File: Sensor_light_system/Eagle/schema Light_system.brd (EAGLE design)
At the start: 80.1 x 49.8 mm, 4 parts

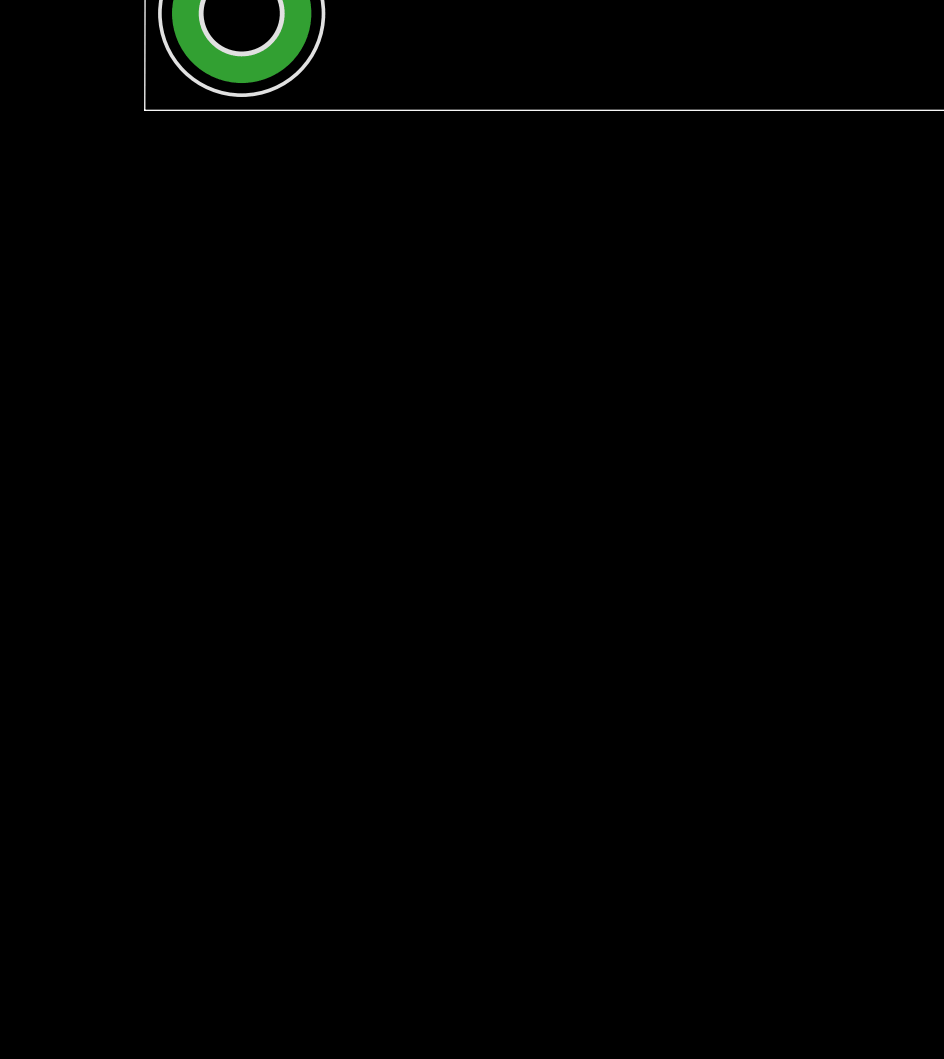
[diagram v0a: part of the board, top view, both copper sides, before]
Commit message: schema sensor aangepast
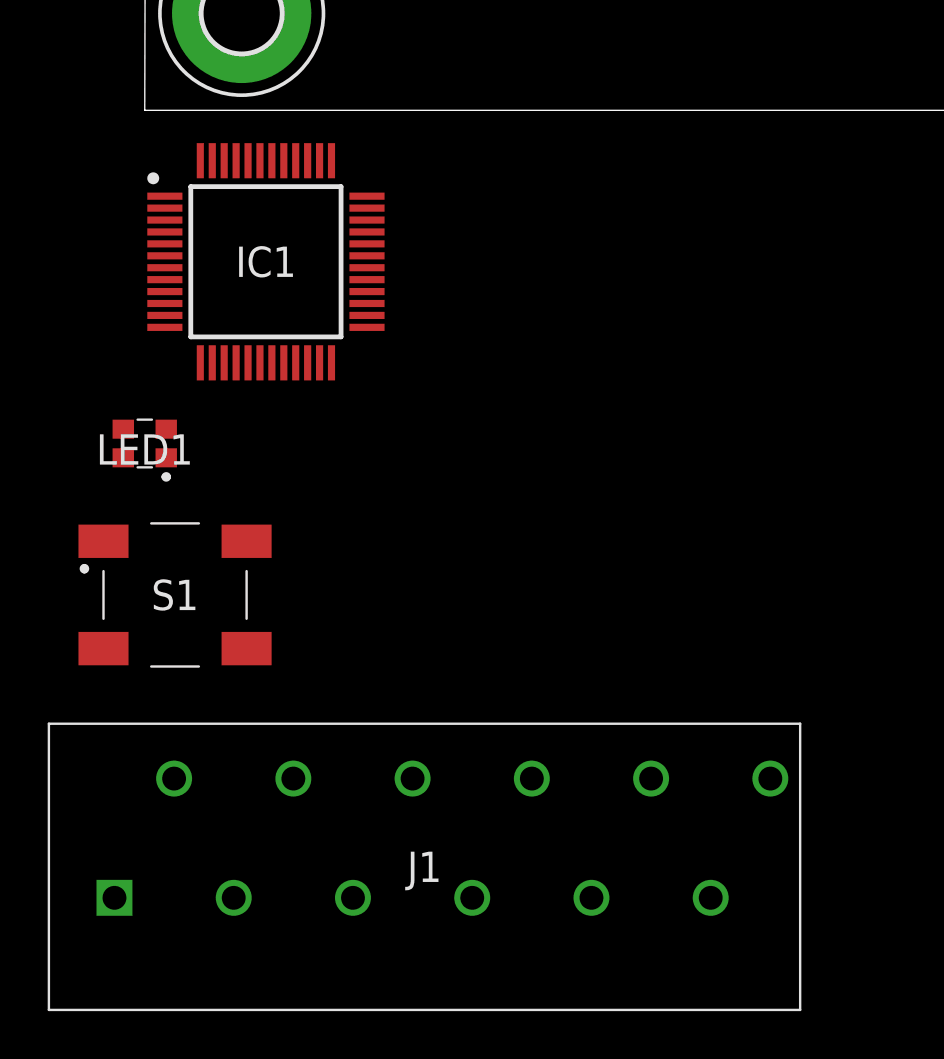
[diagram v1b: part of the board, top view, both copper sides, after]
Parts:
- added IC1: STM32F030C8T6TR, Library light system:QFP50P900X900X160-48N
- added J1: 12_WAY_CON, Library light system:1990106
- added LED1: RGB_LED, Library light system:ASMBKTF00A306
- added S1: PUSH_BUTTON, Library light system:LL3301FF065QJ
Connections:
- new net +3V3: IC1.1, IC1.48
- new net GND: IC1.23
- new net VDDA: IC1.9
- new net VDD_2: IC1.24
- new net VSSA: IC1.8
- new net VSS_2: IC1.47
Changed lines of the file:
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@@
 <element name="H3" library="holes" library_urn="urn:adsk.eagle:library:237" package="3,3-PAD" package3d_urn="urn:adsk.eagle:package:14283/1" value="MOUNT-PAD-ROUND3.3" x="4.064" y="4.064"/>
 <element name="H4" library="holes" library_urn="urn:adsk.eagle:library:237" package="3,3-PAD" package3d_urn="urn:adsk.eagle:package:14283/1" value="MOUNT-PAD-ROUND3.3" x="75.946" y="3.937"/>
+<element name="IC1" library="Library light system" package="QFP50P900X900X160-48N" value="STM32F030C8T6TR" x="5.08" y="-6.35">
+<attribute name="DESCRIPTION" value="32-Bit MCU Cortex-M0 64K Flash LQFP48 32-Bit MCU Cortex-M0 64K Flash LQFP48" x="5.08" y="-6.35" size="1.778" layer="27" display="off"/>
+<attribute name="HEIGHT" value="1.6mm" x="5.08" y="-6.35" size="1.778" layer="27" display="off"/>
+<attribute name="MANUFACTURER_NAME" value="STMicroelectronics" x="5.08" y="-6.35" size="1.778" layer="27" display="off"/>
+<attribute name="MANUFACTURER_PART_NUMBER" value="STM32F030C8T6TR" x="5.08" y="-6.35" size="1.778" layer="27" display="off"/>
+<attribute name="MOUSER_PART_NUMBER" value="511-STM32F030C8T6TR" x="5.08" y="-6.35" size="1.778" layer="27" display="off"/>
+<attribute name="MOUSER_PRICE-STOCK" value="https://www.mouser.com/Search/Refine.aspx?Keyword=511-STM32F030C8T6TR" x="5.08" y="-6.35" size="1.778" layer="27" display="off"/>
+<attribute name="NAME" x="5.08" y="-6.35" size="1.27" layer="25" align="center"/>
+<attribute name="VALUE" x="5.08" y="-6.35" size="1.27" layer="27" align="center"/>
+</element>
+<element name="LED1" library="Library light system" package="ASMBKTF00A306" value="RGB_LED" x="0" y="-13.97">
+<attribute name="DESCRIPTION" value="Standard LEDs - SMD 2220 PLCC4 Tricolor" x="0" y="-13.97" size="1.778" layer="27" display="off"/>
+<attribute name="HEIGHT" value="2.1mm" x="0" y="-13.97" size="1.778" layer="27" display="off"/>
+<attribute name="MANUFACTURER_NAME" value="Avago Technologies" x="0" y="-13.97" size="1.778" layer="27" display="off"/>
+<attribute name="MANUFACTURER_PART_NUMBER" value="ASMB-KTF0-0A306" x="0" y="-13.97" size="1.778" layer="27" display="off"/>
+<attribute name="MOUSER_PART_NUMBER" value="630-ASMB-KTF0-0A306" x="0" y="-13.97" size="1.778" layer="27" display="off"/>
+<attribute name="MOUSER_PRICE-STOCK" value="https://www.mouser.com/Search/Refine.aspx?Keyword=630-ASMB-KTF0-0A306" x="0" y="-13.97" size="1.778" layer="27" display="off"/>
+<attribute name="NAME" x="0" y="-14.22" size="1.27" layer="25" align="center"/>
+<attribute name="VALUE" x="0" y="-14.22" size="1.27" layer="27" align="center"/>
+</element>
+<element name="S1" library="Library light system" package="LL3301FF065QJ" value="PUSH_BUTTON" x="1.27" y="-20.32">
+<attribute name="DESCRIPTION" value="Pushbutton Switches 50mA 12VDC F065 7.0mm J-Lead" x="1.27" y="-20.32" size="1.778" layer="27" display="off"/>
+<attribute name="HEIGHT" value="7.3mm" x="1.27" y="-20.32" size="1.778" layer="27" display="off"/>
+<attribute name="MANUFACTURER_NAME" value="E-Switch" x="1.27" y="-20.32" size="1.778" layer="27" display="off"/>
+<attribute name="MANUFACTURER_PART_NUMBER" value="LL3301FF065QJ" x="1.27" y="-20.32" size="1.778" layer="27" display="off"/>
+<attribute name="MOUSER_PART_NUMBER" value="612-LL3301FF065QJ" x="1.27" y="-20.32" size="1.778" layer="27" display="off"/>
+<attribute name="MOUSER_PRICE-STOCK" value="https://www.mouser.com/Search/Refine.aspx?Keyword=612-LL3301FF065QJ" x="1.27" y="-20.32" size="1.778" layer="27" display="off"/>
+<attribute name="NAME" x="1.27" y="-20.32" size="1.27" layer="25" align="center"/>
+<attribute name="VALUE" x="1.27" y="-20.32" size="1.27" layer="27" align="center"/>
+</element>
+<element name="J1" library="Library light system" package="1990106" value="12_WAY_CON" x="-1.27" y="-33.02">
+<attribute name="DESCRIPTION" value="PTSA 0,5/12-2,5-Z" x="-1.27" y="-33.02" size="1.778" layer="27" display="off"/>
+<attribute name="HEIGHT" value="13.1mm" x="-1.27" y="-33.02" size="1.778" layer="27" display="off"/>
+<attribute name="MANUFACTURER_NAME" value="Phoenix Contact" x="-1.27" y="-33.02" size="1.778" layer="27" display="off"/>
+<attribute name="MANUFACTURER_PART_NUMBER" value="1990106" x="-1.27" y="-33.02" size="1.778" layer="27" display="off"/>
+<attribute name="MOUSER_PART_NUMBER" value="651-1990106" x="-1.27" y="-33.02" size="1.778" layer="27" display="off"/>
+<attribute name="MOUSER_PRICE-STOCK" value="https://www.mouser.com/Search/Refine.aspx?Keyword=651-1990106" x="-1.27" y="-33.02" size="1.778" layer="27" display="off"/>
+<attribute name="NAME" x="11.73" y="-31.72" size="1.27" layer="25" align="center"/>
+<attribute name="VALUE" x="11.73" y="-31.72" size="1.27" layer="27" align="center"/>
+</element>
 </elements>
 <signals>
+<signal name="VSSA">
+<contactref element="IC1" pad="8"/>
+</signal>
+<signal name="VDDA">
+<contactref element="IC1" pad="9"/>
+</signal>
+<signal name="VDD_2">
+<contactref element="IC1" pad="24"/>
+</signal>
+<signal name="VSS_2">
+<contactref element="IC1" pad="47"/>
+</signal>
+<signal name="+3V3">
+<contactref element="IC1" pad="1"/>
+<contactref element="IC1" pad="48"/>
+<wire x1="2.33" y1="-2.112" x2="0.842" y2="-3.6" width="0" layer="19" extent="1-1"/>
+</signal>
+<signal name="GND">
+<contactref element="IC1" pad="23"/>
+</signal>
 </signals>
 <mfgpreviewcolors>

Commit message: schema sensoren
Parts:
- added JP1, JP2, JP3: (no value), jumper:JP4Q
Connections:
- removed net VDDA: IC1.9
- removed net VDD_2: IC1.24
- removed net VSSA: IC1.8
- removed net VSS_2: IC1.47
- new net N$3: IC1.7, S1.3, S1.4
- net +3V3: now also IC1.24, IC1.9
- net GND: now also IC1.47, IC1.8, S1.1, S1.2
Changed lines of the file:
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@@
 <?xml version="1.0" encoding="utf-8"?>
 <!DOCTYPE eagle SYSTEM "eagle.dtd">
-<eagle version="9.2.0">
+<eagle version="8.0.2">
 <drawing>
 <settings>
 <setting alwaysvectorfont="yes"/>
-<setting keepoldvectorfont="yes"/>
 <setting verticaltext="up"/>
 </settings>
@@
 <param name="dpMaxLengthDifference" value="10mm"/>
 <param name="dpGapFactor" value="2.5"/>
+<param name="checkGrid" value="0"/>
 <param name="checkAngle" value="0"/>
 <param name="checkFont" value="1"/>
 <param name="checkRestrict" value="1"/>
-<param name="checkStop" value="0"/>
-<param name="checkValues" value="0"/>
-<param name="checkNames" value="1"/>
-<param name="checkWireStubs" value="1"/>
-<param name="checkPolygonWidth" value="0"/>
 <param name="useDiameter" value="13"/>
 <param name="maxErrors" value="50"/>
@@
 </autorouter>
 <elements>
-<element name="H1" library="holes" library_urn="urn:adsk.eagle:library:237" package="3,3-PAD" package3d_urn="urn:adsk.eagle:package:14283/1" value="MOUNT-PAD-ROUND3.3" x="4.064" y="45.847"/>
-<element name="H2" library="holes" library_urn="urn:adsk.eagle:library:237" package="3,3-PAD" package3d_urn="urn:adsk.eagle:package:14283/1" value="MOUNT-PAD-ROUND3.3" x="76.073" y="45.72"/>
-<element name="H3" library="holes" library_urn="urn:adsk.eagle:library:237" package="3,3-PAD" package3d_urn="urn:adsk.eagle:package:14283/1" value="MOUNT-PAD-ROUND3.3" x="4.064" y="4.064"/>
-<element name="H4" library="holes" library_urn="urn:adsk.eagle:library:237" package="3,3-PAD" package3d_urn="urn:adsk.eagle:package:14283/1" value="MOUNT-PAD-ROUND3.3" x="75.946" y="3.937"/>
+<element name="H1" library="holes" package="3,3-PAD" value="MOUNT-PAD-ROUND3.3" x="4.064" y="45.847"/>
+<element name="H2" library="holes" package="3,3-PAD" value="MOUNT-PAD-ROUND3.3" x="76.073" y="45.72"/>
+<element name="H3" library="holes" package="3,3-PAD" value="MOUNT-PAD-ROUND3.3" x="4.064" y="4.064"/>
+<element name="H4" library="holes" package="3,3-PAD" value="MOUNT-PAD-ROUND3.3" x="75.946" y="3.937"/>
 <element name="IC1" library="Library light system" package="QFP50P900X900X160-48N" value="STM32F030C8T6TR" x="5.08" y="-6.35">
 <attribute name="DESCRIPTION" value="32-Bit MCU Cortex-M0 64K Flash LQFP48 32-Bit MCU Cortex-M0 64K Flash LQFP48" x="5.08" y="-6.35" size="1.778" layer="27" display="off"/>
@@
 <attribute name="VALUE" x="11.73" y="-31.72" size="1.27" layer="27" align="center"/>
 </element>
+<element name="JP1" library="jumper" package="JP4Q" value="" x="-13.97" y="-49.53"/>
+<element name="JP2" library="jumper" package="JP4Q" value="" x="-13.97" y="-67.31"/>
+<element name="JP3" library="jumper" package="JP4Q" value="" x="-13.97" y="-85.09"/>
 </elements>
 <signals>
-<signal name="VSSA">
-<contactref element="IC1" pad="8"/>
-</signal>
-<signal name="VDDA">
-<contactref element="IC1" pad="9"/>
-</signal>
-<signal name="VDD_2">
-<contactref element="IC1" pad="24"/>
-</signal>
-<signal name="VSS_2">
-<contactref element="IC1" pad="47"/>
-</signal>
 <signal name="+3V3">
 <contactref element="IC1" pad="1"/>
 <contactref element="IC1" pad="48"/>
+<contactref element="IC1" pad="9"/>
+<contactref element="IC1" pad="24"/>
+<wire x1="0.842" y1="-3.6" x2="0.842" y2="-7.6" width="0" layer="19" extent="1-1"/>
 <wire x1="2.33" y1="-2.112" x2="0.842" y2="-3.6" width="0" layer="19" extent="1-1"/>
+<wire x1="7.83" y1="-10.588" x2="0.842" y2="-7.6" width="0" layer="19" extent="1-1"/>
 </signal>
 <signal name="GND">
 <contactref element="IC1" pad="23"/>
+<contactref element="IC1" pad="8"/>
+<contactref element="IC1" pad="47"/>
+<contactref element="S1" pad="2"/>
+<contactref element="S1" pad="1"/>
+<wire x1="4.27" y1="-18.07" x2="-1.73" y2="-18.07" width="0" layer="19" extent="1-1"/>
+<wire x1="7.33" y1="-10.588" x2="4.27" y2="-18.07" width="0" layer="19" extent="1-1"/>
+<wire x1="0.842" y1="-7.1" x2="7.33" y2="-10.588" width="0" layer="19" extent="1-1"/>
+<wire x1="2.83" y1="-2.112" x2="0.842" y2="-7.1" width="0" layer="19" extent="1-1"/>
+</signal>
+<signal name="N$3">
+<contactref element="S1" pad="4"/>
+<contactref element="S1" pad="3"/>
+<contactref element="IC1" pad="7"/>
+<wire x1="4.27" y1="-22.57" x2="-1.73" y2="-22.57" width="0" layer="19" extent="1-1"/>
+<wire x1="0.842" y1="-6.6" x2="-1.73" y2="-22.57" width="0" layer="19" extent="1-1"/>
 </signal>
 </signals>
-<mfgpreviewcolors>
-<mfgpreviewcolor name="soldermaskcolor" color="0xC8008000"/>
-<mfgpreviewcolor name="silkscreencolor" color="0xFFFEFEFE"/>
-<mfgpreviewcolor name="backgroundcolor" color="0xFF282828"/>
-<mfgpreviewcolor name="coppercolor" color="0xFFFFBF00"/>
-<mfgpreviewcolor name="substratecolor" color="0xFF786E46"/>
-</mfgpreviewcolors>
 </board>
 </drawing>
-<compatibility>
-<note version="8.2" severity="warning">
-Since Version 8.2, EAGLE supports online libraries. The ids
-of those online libraries will not be understood (or retained)
-with this version.
-</note>
-<note version="8.3" severity="warning">
-Since Version 8.3, EAGLE supports URNs for individual library
-assets (packages, symbols, and devices). The URNs of those assets
-will not be understood (or retained) with this version.
-</note>
-<note version="8.3" severity="warning">
-Since Version 8.3, EAGLE supports the association of 3D packages
-with devices in libraries, schematics, and board files. Those 3D
-packages will not be understood (or retained) with this version.
-</note>
-</compatibility>
 </eagle>

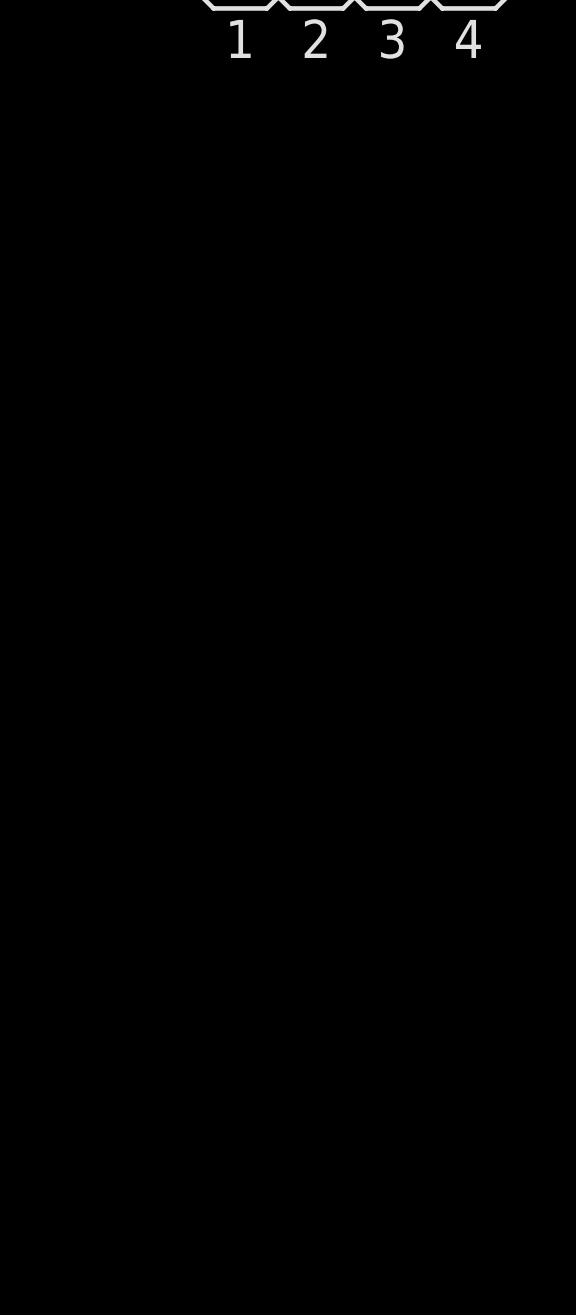
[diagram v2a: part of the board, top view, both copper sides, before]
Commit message: schema sensor
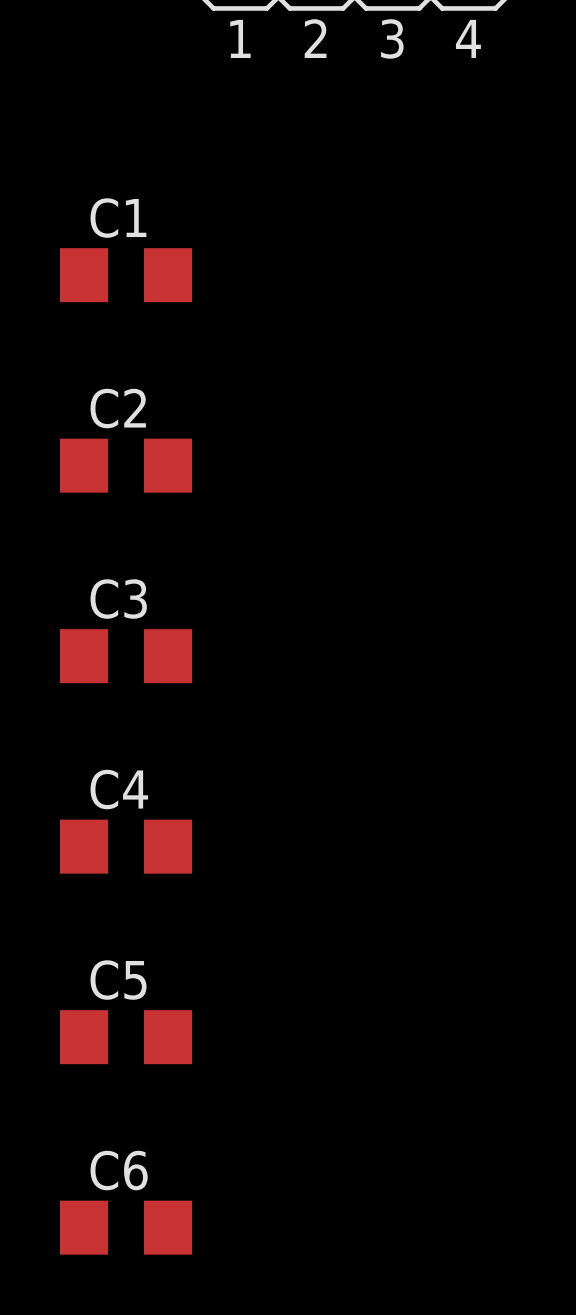
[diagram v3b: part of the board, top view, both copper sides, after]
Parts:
- added C1, C2, C3, C4, C5, C6: 100nF, resistor:C1206
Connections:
- net +3V3: now also C2.2, C3.2, C4.2, C5.2, C6.2, JP1.1, JP2.1, JP3.1
- net GND: now also C1.1, C2.1, C3.1, C4.1, C5.1, C6.1, JP1.8, JP2.8, JP3.8
- net N$3: now also C1.2
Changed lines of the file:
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@@
 <element name="JP2" library="jumper" package="JP4Q" value="" x="-13.97" y="-67.31"/>
 <element name="JP3" library="jumper" package="JP4Q" value="" x="-13.97" y="-85.09"/>
+<element name="C1" library="resistor" package="C1206" value="100nF" x="-21.59" y="-96.52"/>
+<element name="C2" library="resistor" package="C1206" value="100nF" x="-21.59" y="-102.87"/>
+<element name="C3" library="resistor" package="C1206" value="100nF" x="-21.59" y="-109.22"/>
+<element name="C4" library="resistor" package="C1206" value="100nF" x="-21.59" y="-115.57"/>
+<element name="C5" library="resistor" package="C1206" value="100nF" x="-21.59" y="-121.92"/>
+<element name="C6" library="resistor" package="C1206" value="100nF" x="-21.59" y="-128.27"/>
 </elements>
 <signals>
@@
 <contactref element="IC1" pad="9"/>
 <contactref element="IC1" pad="24"/>
+<contactref element="JP1" pad="1"/>
+<contactref element="C2" pad="2"/>
+<contactref element="C6" pad="2"/>
+<contactref element="C5" pad="2"/>
+<contactref element="C4" pad="2"/>
+<contactref element="C3" pad="2"/>
+<contactref element="JP2" pad="1"/>
+<contactref element="JP3" pad="1"/>
+<wire x1="-20.19" y1="-121.92" x2="-20.19" y2="-128.27" width="0" layer="19" extent="1-1"/>
+<wire x1="-20.19" y1="-115.57" x2="-20.19" y2="-121.92" width="0" layer="19" extent="1-1"/>
+<wire x1="-20.19" y1="-109.22" x2="-20.19" y2="-115.57" width="0" layer="19" extent="1-1"/>
+<wire x1="-20.19" y1="-102.87" x2="-20.19" y2="-109.22" width="0" layer="19" extent="1-1"/>
+<wire x1="-17.78" y1="-86.36" x2="-20.19" y2="-102.87" width="0" layer="19" extent="1-1"/>
+<wire x1="-17.78" y1="-68.58" x2="-17.78" y2="-86.36" width="0" layer="19" extent="1-1"/>
+<wire x1="-17.78" y1="-50.8" x2="-17.78" y2="-68.58" width="0" layer="19" extent="1-1"/>
+<wire x1="0.842" y1="-7.6" x2="-17.78" y2="-50.8" width="0" layer="19" extent="1-1"/>
 <wire x1="0.842" y1="-3.6" x2="0.842" y2="-7.6" width="0" layer="19" extent="1-1"/>
 <wire x1="2.33" y1="-2.112" x2="0.842" y2="-3.6" width="0" layer="19" extent="1-1"/>
@@
 <contactref element="S1" pad="2"/>
 <contactref element="S1" pad="1"/>
+<contactref element="JP1" pad="8"/>
+<contactref element="C1" pad="1"/>
+<contactref element="C4" pad="1"/>
+<contactref element="C5" pad="1"/>
+<contactref element="C2" pad="1"/>
+<contactref element="C6" pad="1"/>
+<contactref element="C3" pad="1"/>
+<contactref element="JP2" pad="8"/>
+<contactref element="JP3" pad="8"/>
+<wire x1="-22.99" y1="-121.92" x2="-22.99" y2="-128.27" width="0" layer="19" extent="1-1"/>
+<wire x1="-22.99" y1="-115.57" x2="-22.99" y2="-121.92" width="0" layer="19" extent="1-1"/>
+<wire x1="-22.99" y1="-109.22" x2="-22.99" y2="-115.57" width="0" layer="19" extent="1-1"/>
+<wire x1="-22.99" y1="-102.87" x2="-22.99" y2="-109.22" width="0" layer="19" extent="1-1"/>
+<wire x1="-22.99" y1="-96.52" x2="-22.99" y2="-102.87" width="0" layer="19" extent="1-1"/>
+<wire x1="-10.16" y1="-83.82" x2="-22.99" y2="-96.52" width="0" layer="19" extent="1-1"/>
+<wire x1="-10.16" y1="-66.04" x2="-10.16" y2="-83.82" width="0" layer="19" extent="1-1"/>
+<wire x1="-10.16" y1="-48.26" x2="-10.16" y2="-66.04" width="0" layer="19" extent="1-1"/>
+<wire x1="-1.73" y1="-18.07" x2="-10.16" y2="-48.26" width="0" layer="19" extent="1-1"/>
 <wire x1="4.27" y1="-18.07" x2="-1.73" y2="-18.07" width="0" layer="19" extent="1-1"/>
 <wire x1="7.33" y1="-10.588" x2="4.27" y2="-18.07" width="0" layer="19" extent="1-1"/>
@@
 <contactref element="S1" pad="3"/>
 <contactref element="IC1" pad="7"/>
+<contactref element="C1" pad="2"/>
+<wire x1="-1.73" y1="-22.57" x2="-20.19" y2="-96.52" width="0" layer="19" extent="1-1"/>
 <wire x1="4.27" y1="-22.57" x2="-1.73" y2="-22.57" width="0" layer="19" extent="1-1"/>
 <wire x1="0.842" y1="-6.6" x2="-1.73" y2="-22.57" width="0" layer="19" extent="1-1"/>
